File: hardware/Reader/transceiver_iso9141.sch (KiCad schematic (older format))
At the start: 15 parts, among them Q2 IRLML5103TRPBF, Q3 MMBT3904WT1G, Q4 IRLML5103TRPBF, Q5 MMBT3904WT1G

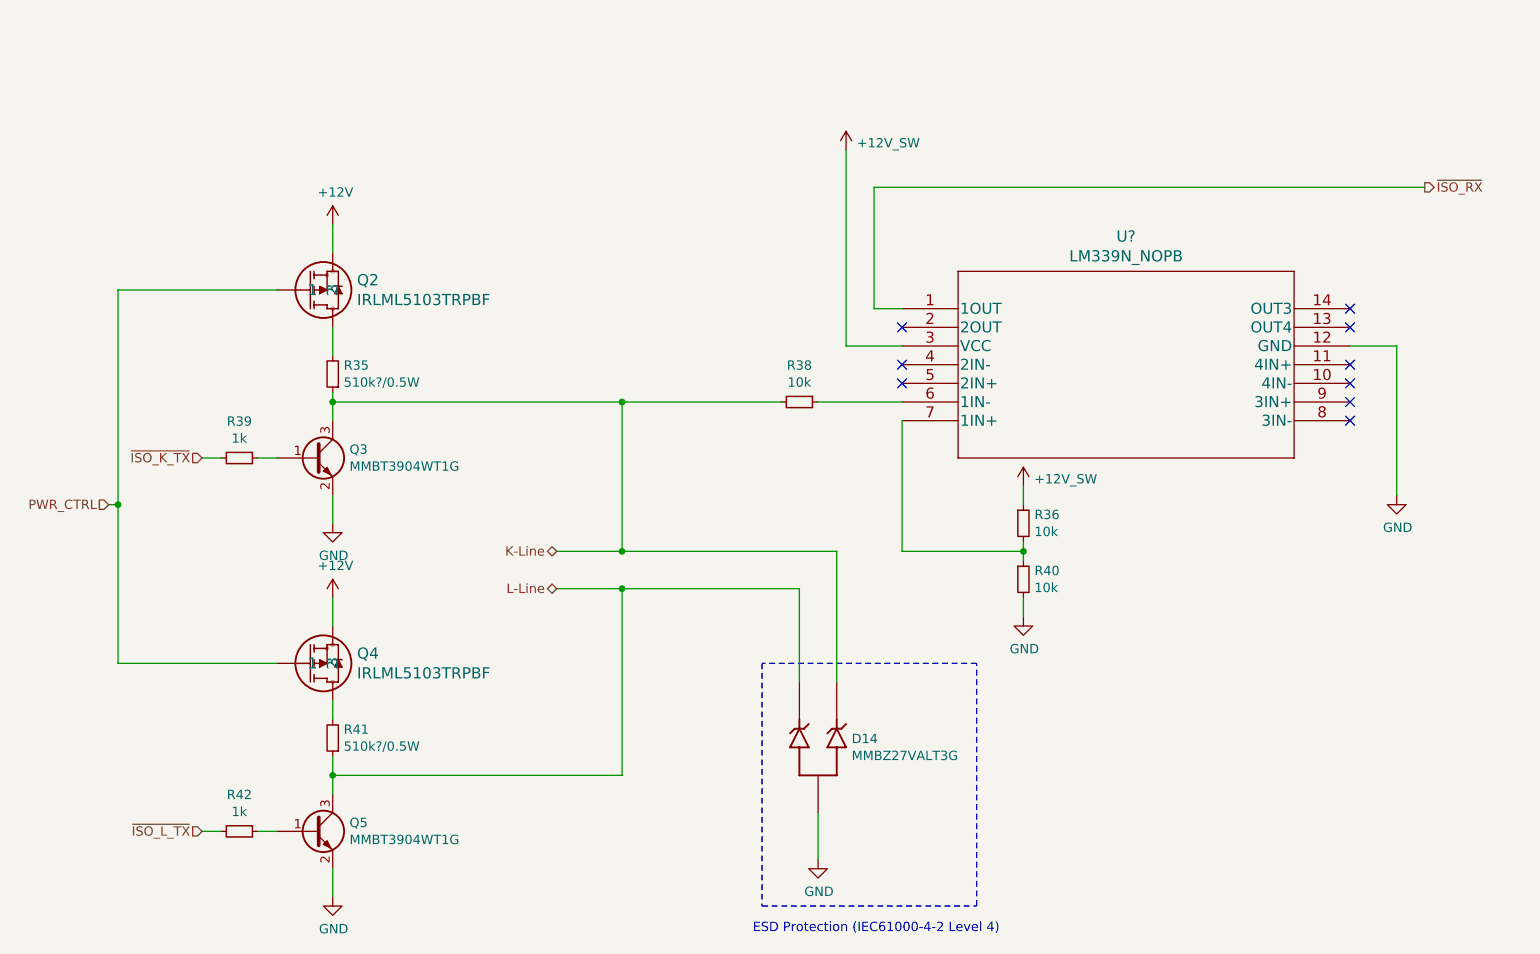
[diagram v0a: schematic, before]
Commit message: Completed schematics for reader
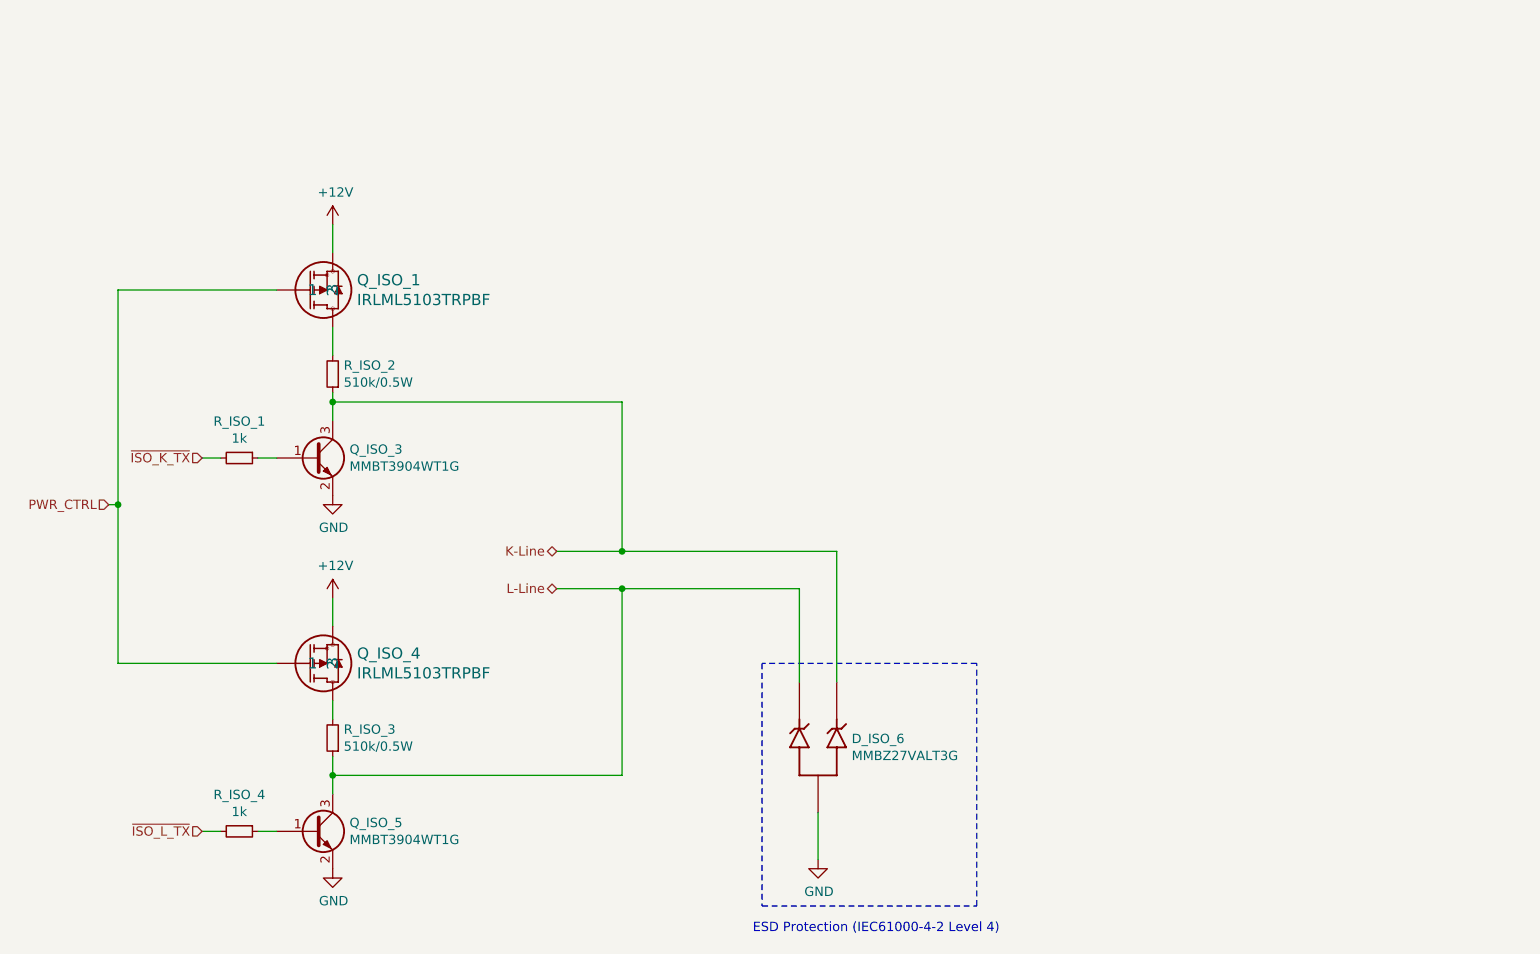
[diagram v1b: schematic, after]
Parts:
- removed PWR? (x2): +12V_SW, symbol CANtech:+12V_SW
- removed R36, R38, R40: 10k, symbol Device:R_Small
- removed U?: LM339N_NOPB, N14_TEX, symbol LM339NNOPB:LM339N_NOPB
- Q_ISO_1: renamed from Q2; footprint MICRO3_SOT23_INF -> footprints:IRLML5103TRPBF
- Q_ISO_4: renamed from Q4; footprint MICRO3_SOT23_INF -> footprints:IRLML5103TRPBF
- R_ISO_1: renamed from R39; footprint (none) -> footprints:RC1608F102CS; Part Name (none) -> RC1608F102CS
- R_ISO_2: renamed from R35; value 510k?/0.5W -> 510k/0.5W; footprint (none) -> footprints:RESC2012X70N; Part Name (none) -> ERJ-P06J514V
- R_ISO_3: renamed from R41; value 510k?/0.5W -> 510k/0.5W; footprint (none) -> footprints:RESC2012X70N; Part Name (none) -> ERJ-P06J514V
- R_ISO_4: renamed from R42; footprint (none) -> footprints:RC1608F102CS; Part Name (none) -> RC1608F102CS
- renumbered D14 to D_ISO_6, Q3 to Q_ISO_3, Q5 to Q_ISO_5
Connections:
- no-connect marks 9 -> 0

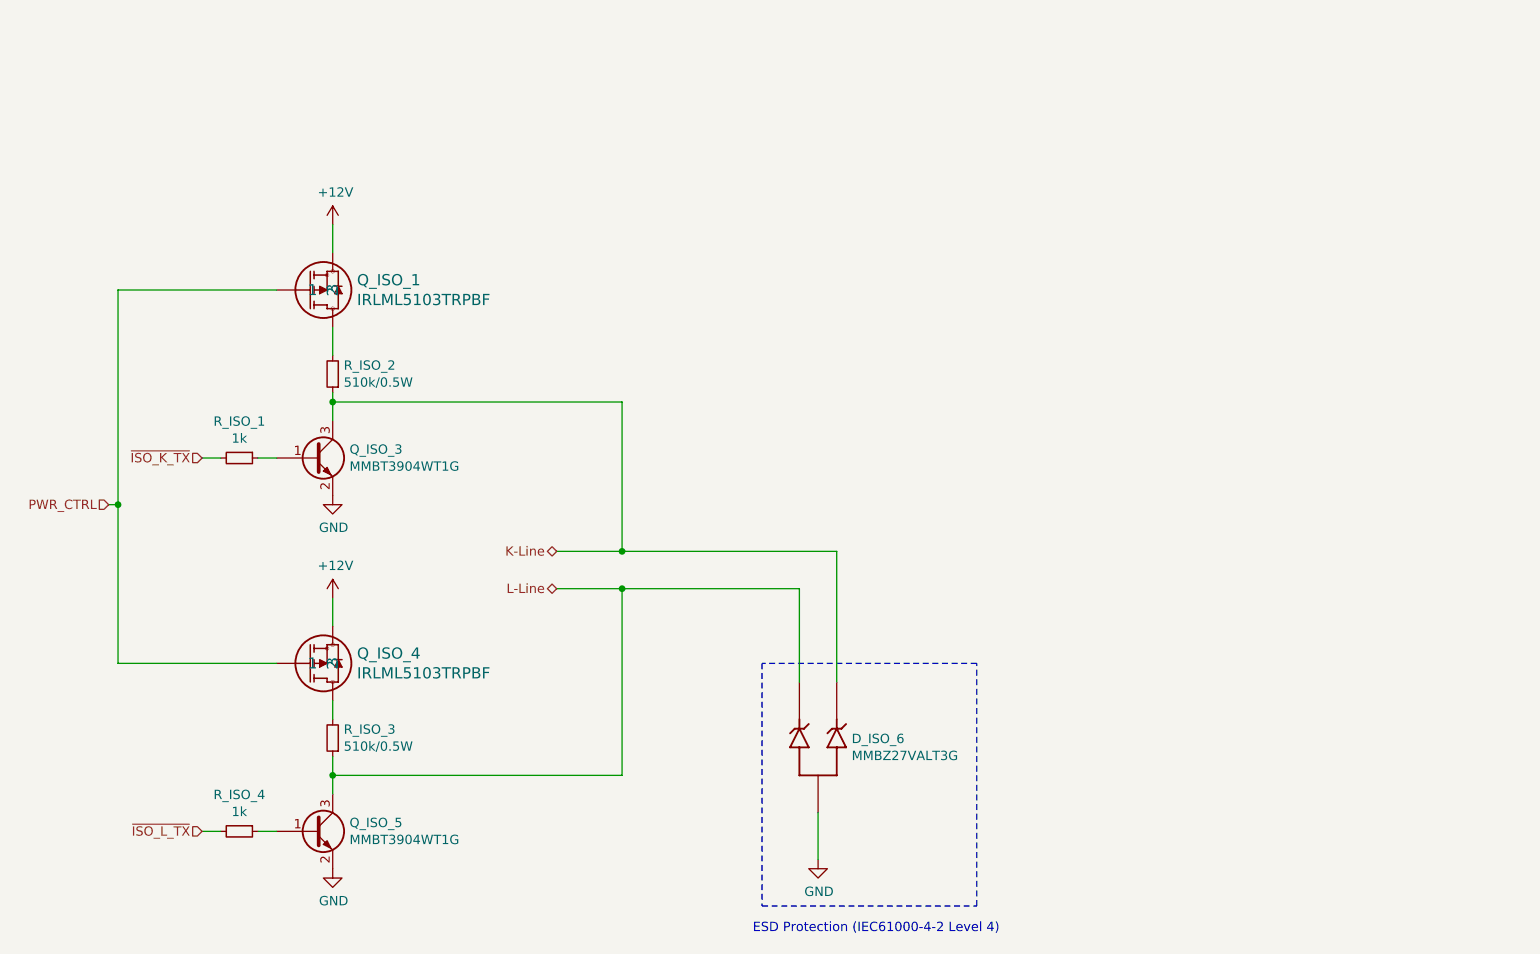
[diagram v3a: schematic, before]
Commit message: Added ESD Protection. Fixed minor bugs on schematic. Attempted placement of components
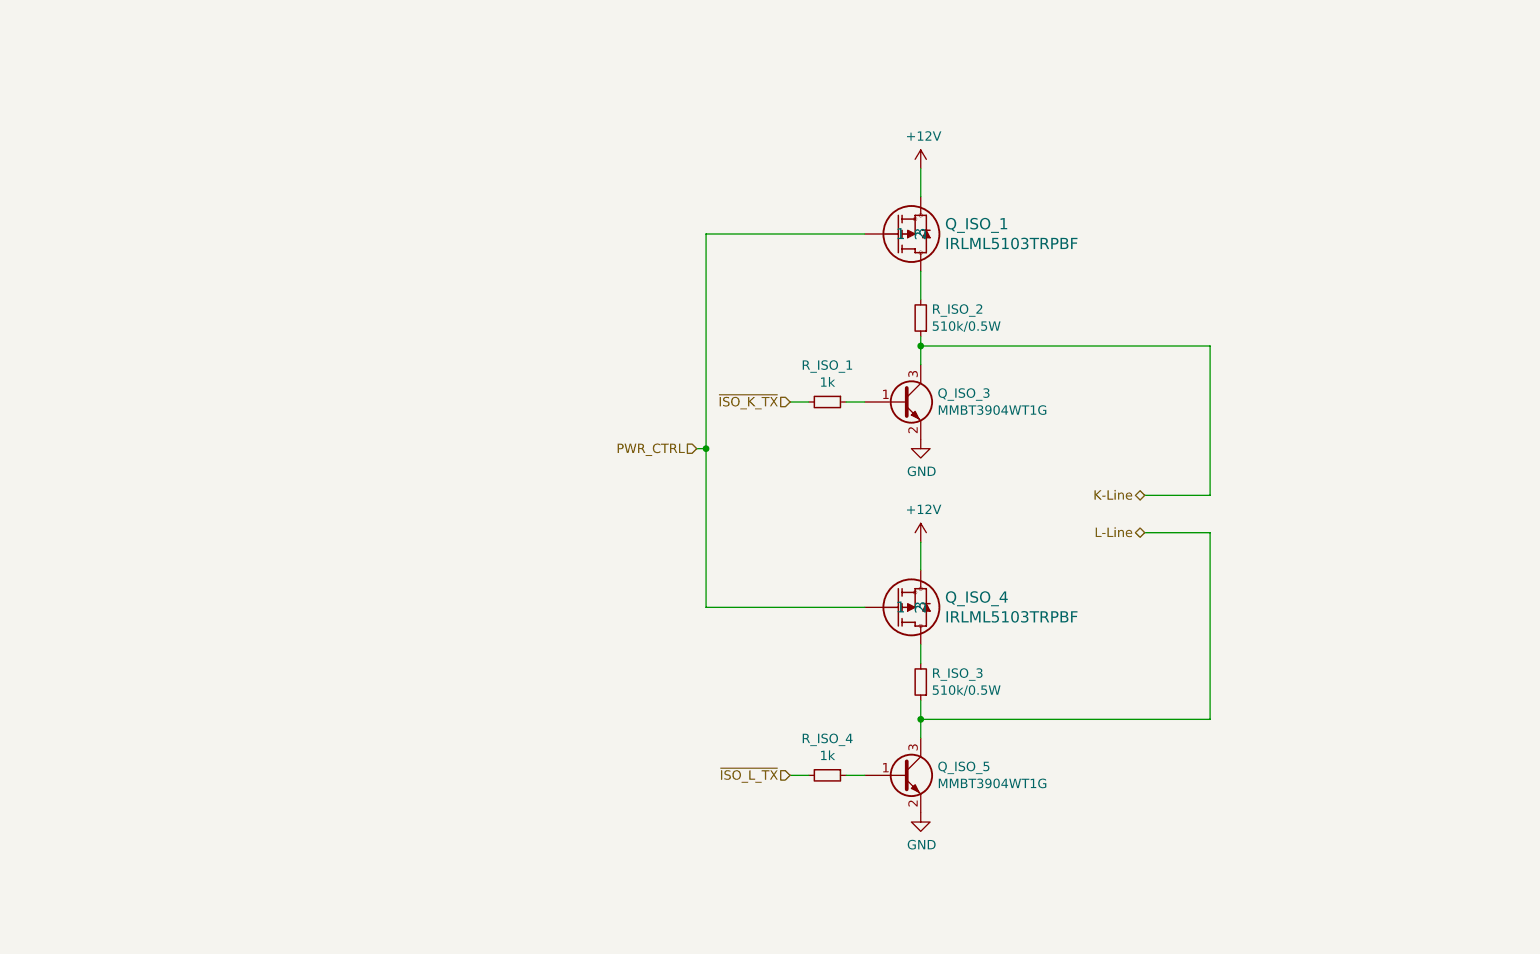
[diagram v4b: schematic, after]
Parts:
- removed D_ISO_6: MMBZ27VALT3G, SOT95P237X111-3N, symbol MMBZ27VALT3G:MMBZ27VALT3G
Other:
- note removed: "ESD Protection (IEC61000-4-2 Level 4)"
- moved on the sheet: Q_ISO_1, Q_ISO_3, Q_ISO_4, Q_ISO_5, R_ISO_1, R_ISO_2, R_ISO_3, R_ISO_4
